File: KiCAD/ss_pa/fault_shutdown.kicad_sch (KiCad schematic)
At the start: 0 parts

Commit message: KiCad revC: ss_pa fault_shutdown populated + CD74HC4066 symbol + doc
Fault_shutdown sheet implemented with the self-latching V_REF scheme:
- LM393 (U1) powered from +3.3V (via RJ45 pin 6 from analog board)
- V_REF divider (R11=100K, R10=10K) powered from FAULT_N bus, giving
  intrinsic self-latching when fault asserts (no flip-flop needed) —
  normal V_REF ≈ 288 mV, fault V_REF = 0
- Pullup R9 (4.7K) on FAULT_N to +3.3V, wire-OR of both LM393 outputs
- FAULT_N is active-low (user renamed from FAULT after wire-OR polarity
  analysis — open-collector wire-OR of multiple fault sources requires
  LOW = fault for proper OR behavior)
- Startup cap C12 (1uF) + D1 (1N4148, cathode to V_REF) auto-resets
  the latch at power-on without needing button press
- CD74HC4066 (U2) in series with Bias_A/Bias_B lines — control pins
  tied to FAULT_N (HIGH=closed, LOW=open). Series-pass approach
  (not shunt-to-GND) avoids loading the MCP4728 DAC during a latched
  fault
- Reset: J5 screw terminal for external pushbutton; shorts +3.3V to
  V_REF momentarily to break the latch
- Noise filtering: C11 (0.01uF) on FAULT_N bus; C14/C15 (0.1uF each)
  bypass caps for U1 and U2
- RJ45 J7 (Amphenol RJE1D-188 shielded 8P8C) per T568B pair plan;
  shield grounded on PA-board end only

PA stage additions since last commit:
- L5 (12 uH on FT50-43, 5-6 turns) — supply input RFC between J2
  power entry and the +13.8V bus (L201-equivalent per QRP Labs kit)
- Fixed earlier wiring bugs flagged in review: U1 pin 6 moved from
  Source_Sense_A to Source_Sense_B so comparator B monitors Q4; C13
  replaced by C15 wired correctly as U2 bypass cap

Library:
- Added CD74HC4066 symbol (PDIP-14) to xmitter.kicad_sym with
  TI-style pinout; footprint = Package_DIP:DIP-14_W7.62mm

Documentation:
- Documentation/ss_pa.md rewritten to reflect as-built design:
  updated RJ45 pin assignment (pin 6 = +3.3V, pin 3 = FAULT_N),
  added L5 to supply decoupling, full rewrite of fault_shutdown
  section with the self-latchi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
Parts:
- added C11: 0.01uF, symbol Device:C
- added C12: 1uF, symbol Device:C
- added C14, C15: 0.1uF, symbol Device:C
- added D1: 1N4148, Diode_THT:D_DO-35_SOD27_P7.62mm_Horizontal, symbol Diode:1N4148
- added J5: Screw_Terminal_01x02, symbol Connector:Screw_Terminal_01x02
- added J7: 8P8C_Shielded, xmitter:Amphenol_RJE1D-188_Horizontal_Shielded, symbol Connector:8P8C_Shielded
- added R10: 10K, symbol Device:R_US
- added R11: 100K, symbol Device:R_US
- added R9: 4.7K, symbol Device:R_US
- added U1: LM393, symbol Comparator:LM393
- added U2: CD74HC4066, Package_DIP:DIP-14_W7.62mm, symbol xmitter:CD74HC4066
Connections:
- new net: C12.1, D1.2 (A)
- new net +3.3V: C12.2, C14.2, C15.2, J5.1 (Pin_1), J7.6, R9.1, U1.8 (V+), U2.14 (VCC)
- new net Bias_A: U2.2 (1Z)
- new net Bias_A_Raw: J7.7, U2.1 (1Y)
- new net Bias_B: U2.3 (2Z)
- new net Bias_B_Raw: J7.8, U2.4 (2Y)
- new net FAULT_N: C11.1, J7.3, R11.1, R9.2, U1.1, U1.7, U2.13 (1E), U2.5 (2E)
- new net GND: C11.2, C14.1, C15.1, J7.2, J7.5, J7.SH, R10.2, U1.4 (V-), U2.10 (4Z), U2.11 (4Y), U2.12 (4E), U2.6 (3E), U2.7 (GND), U2.8 (3Y), U2.9 (3Z)
- new net Source_Sense_A: J7.1, U1.2 (-)
- new net Source_Sense_B: J7.4, U1.6 (-)
- new net V_REF: D1.1 (K), J5.2 (Pin_2), R10.1, R11.2, U1.3 (+), U1.5 (+)
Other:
- note added: "If either source exceeds V_REF FAULT_N goes low"
- note added: "To pushbutton for manual reset"

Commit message: revC: accumulated schematic/netlist updates + BOM tooling
- analog + ss_pa netlists regenerated to current schematic state
- interface/arduino/dac/power sheet updates on analog
- fault_shutdown and pa_stage edits on ss_pa (footprint assignments)
- assign_cap_footprints.py: additional VALUE_TO_FOOTPRINT entries
- gen_board_boms.py: per-board BOM generator (multi-sheet .xlsx by
  component category, first-match-wins bucketing, DNP exclusion)
- gen_total_bom.py: consolidated BOM across analog + frontpanel + ss_pa
  for a single Mouser order, board-prefixed references, mixed-footprint
  flagging per Value row

Co-Authored-By: Claude Opus 4.7 <noreply@anthropic.com>
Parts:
- C11: footprint (none) -> Capacitor_THT:C_Disc_D6.0mm_W2.5mm_P5.00mm
- C12: footprint (none) -> Capacitor_THT:C_Rect_L7.2mm_W4.5mm_P5.00mm
- C14, C15: footprint (none) -> Capacitor_THT:C_Disc_D5.0mm_W2.5mm_P5.00mm
- J5: footprint (none) -> TerminalBlock_Phoenix:TerminalBlock_Phoenix_MKDS-1,5-2_1x02_P5.00mm_Horizontal
- R10, R11, R9: footprint (none) -> Resistor_THT:R_Axial_DIN0207_L6.3mm_D2.5mm_P10.16mm_Horizontal
- U1: footprint (none) -> Package_DIP:DIP-8_W7.62mm
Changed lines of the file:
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@@
 			)
 		)
-		(property "Footprint" ""
+		(property "Footprint" "Package_DIP:DIP-8_W7.62mm"
 			(at 115.57 129.54 0)
 			(hide yes)
@@
 			)
 		)
-		(property "Footprint" ""
+		(property "Footprint" "Capacitor_THT:C_Disc_D6.0mm_W2.5mm_P5.00mm"
 			(at 136.8552 156.21 0)
 			(hide yes)
@@
 			)
 		)
-		(property "Footprint" ""
+		(property "Footprint" "Capacitor_THT:C_Disc_D5.0mm_W2.5mm_P5.00mm"
 			(at 107.95 142.5448 0)
 			(hide yes)
@@
 			)
 		)
-		(property "Footprint" ""
+		(property "Footprint" "Resistor_THT:R_Axial_DIN0207_L6.3mm_D2.5mm_P10.16mm_Horizontal"
 			(at 131.826 109.474 90)
 			(hide yes)
@@
 			)
 		)
-		(property "Footprint" ""
+		(property "Footprint" "Capacitor_THT:C_Rect_L7.2mm_W4.5mm_P5.00mm"
 			(at 172.4152 158.75 0)
 			(hide yes)
@@
 			)
 		)
-		(property "Footprint" ""
+		(property "Footprint" "Package_DIP:DIP-8_W7.62mm"
 			(at 114.3 151.13 0)
 			(hide yes)
@@
 			)
 		)
-		(property "Footprint" ""
+		(property "Footprint" "TerminalBlock_Phoenix:TerminalBlock_Phoenix_MKDS-1,5-2_1x02_P5.00mm_Horizontal"
 			(at 185.42 140.97 0)
 			(hide yes)
@@
 			)
 		)
-		(property "Footprint" ""
+		(property "Footprint" "Resistor_THT:R_Axial_DIN0207_L6.3mm_D2.5mm_P10.16mm_Horizontal"
 			(at 143.764 147.574 90)
 			(hide yes)
@@
 			)
 		)
-		(property "Footprint" ""
+		(property "Footprint" "Capacitor_THT:C_Disc_D5.0mm_W2.5mm_P5.00mm"
 			(at 160.9852 69.85 0)
 			(hide yes)
@@
 			)
 		)
-		(property "Footprint" ""
+		(property "Footprint" "Package_DIP:DIP-8_W7.62mm"
 			(at 115.57 113.03 0)
 			(hide yes)
@@
 			)
 		)
-		(property "Footprint" ""
+		(property "Footprint" "Resistor_THT:R_Axial_DIN0207_L6.3mm_D2.5mm_P10.16mm_Horizontal"
 			(at 150.876 153.924 90)
 			(hide yes)

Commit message: revD: DGFET-DAC bias scheme, kit-style xfmr naming, custom footprints, Output LPF project
Architecture refinements since the previous revD commit (f8d7058):

Analog board (vfo_complete, arduino, dac, power sheets):
  * MCP4922 (U4) ch B exposed as DRIVER_BIAS DAC output -> J31 pin 6
    (replaces the +3.3V pin that was on J31 pin 6 before). Analog's U4
    now controls the ss_pa BS170 driver DC bias point directly from
    firmware -- cleaner than the kit's trimmer+Q201 scheme.
  * MCP4728 (U3) ch A/B exposed as PA_Bias_A_Raw / PA_Bias_B_Raw ->
    J31 pins 7, 8. These feed the ss_pa CD74HC4066 fault-switch (U2),
    which gates them to PA_Bias_A/B on the IRF510 gates. On FAULT_N
    low, switch opens -> IRF510 bias collapses -> conduction cuts.
  * Rename pass: Bias_A/B/_Raw labels -> PA_Bias_A/B/_Raw everywhere
    (analog J3 screw-terminal, umbilical J31, ss_pa U2 inputs). Prefix
    disambiguates from DRIVER_BIAS which drives a different stage.
  * J2 (band-select RJ45 to Output LPF board): added RLY_40 provision.
    Pin layout reorganized -- RLY_40 lives at pin 5, pin 6 kept as a
    spare for a future 6th band.

ss_pa board (pa_stage, fault_shutdown, lpf sheets):
  * Driver + final BS170/IRF510 topology drawn following QRP Labs
    10W Linear kit (RF IN -> T201 input xfmr -> BS170 PP driver
    (Q2, Q6) -> T202 interstage -> IRF510 PP finals (Q3, Q4) ->
    T203 bifilar drain feed -> T204 output xfmr -> RF out).
  * Transformer references renamed to match the kit: T201 (input,
    BN61-2402), T202 (interstage, BN61-2402), T203 (drain feed,
    T50-43), T204 (output, BN43-202).
  * Driver bias filter on DRIVER_BIAS: C19 (0.1uF) + C20 (100pF)
    bulk + HF bypass, into T201 secondary CT (pin 4).
  * +3.3V now locally regulated on ss_pa (MCP1700x-330xxTO, U13)
    from +13.8V, powering U1 (LM393) and U2 (CD74HC4066). J31
    pin 6 freed up for DRIVER_BIAS.
  * Duplicate RJ45 J7 deleted (was a leftover from pre-DAC-bias era).
  * J3 (SMA RF input from analog) foo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
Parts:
- removed J7: 8P8C_Shielded, xmitter:Amphenol_RJE1D-188_Horizontal_Shielded, symbol Connector:8P8C_Shielded
- added C16, C21: 1uF, Capacitor_THT:C_Rect_L7.2mm_W4.5mm_P5.00mm, symbol Device:C_US
- added R12, R19: 100K, Resistor_THT:R_Axial_DIN0207_L6.3mm_D2.5mm_P10.16mm_Horizontal, symbol Device:R_US
- added U13: MCP1700x-330xxTO, Package_TO_SOT_THT:TO-92_Inline_Wide, symbol Regulator_Linear:MCP1700x-330xxTO
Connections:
- net +3.3V: now also C21.1, U13.3 (VO)
- net GND: now also C16.2, C21.2, R12.2, R19.1, U13.1 (GND)
- net Bias_A renamed PA_Bias_A
- net PA_Bias_A: now also R19.2
- net Bias_A_Raw renamed PA_Bias_A_Raw
- net Bias_B renamed PA_Bias_B
- net PA_Bias_B: now also R12.1
- net Bias_B_Raw renamed PA_Bias_B_Raw
- new net +13.8V: C16.1, U13.2 (VI)

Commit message: revD ss_pa: add test points (drains + RF out + bias + supply), 4-layer PCB
ss_pa test points added:
  TP1  +3.3V          - local U13 LDO output monitor
  TP2  PA_Bias_A      - IRF510 Q3 bias after fault switch (R12 pulldown)
  TP3  PA_Bias_B      - IRF510 Q4 bias after fault switch (R19 pulldown)
  TP4  (unconnected)  - orphan pad, clean up in next pass
  TP5  RF OUT         - J1 center pin, final 50 ohm matched RF out
  TP6  Q3 drain       - hot RF, oscillation check pad
  TP7  Q4 drain       - hot RF, oscillation check pad
  TP8  GND            - probe-return pad near one hot-RF TP
  TP9  GND            - probe-return pad near other hot-RF TP

Deliberately minimal set per earlier RF-stability discussion:
  * No TPs on BS170 drains, IRF510 gates, driver sources, or J3 RF
    input -- would require longer stubs that risk disturbing the
    VHF-tuned drain-gate feedback network. Mini-grabber on the
    device lead during bring-up is cleaner than a permanent pad.
  * Hot-RF TPs (TP5/6/7) are small-pad / short-stub.
  * Each hot-RF TP is paired with a nearby GND pad (TP8, TP9) so
    scope-probe ground spring reaches directly -- short probe loop
    for clean HF waveform, no antenna pickup.

4-layer PCB stackup planned for ss_pa (not 2-layer):
  * Outer layers: signal + GND pour
  * Inner layer 2: solid GND plane (uninterrupted)
  * Inner layer 3: solid +13.8 V plane (uninterrupted)
  * Via-stitching ties outer GND pours to inner GND plane
Benefits: cleaner RF return currents under driver + final chain,
lower-impedance power distribution for IRF510 pulse currents
(~2 A peak each), better heat spreading through +13.8 V plane
under the drain-feed region, reduced EMI radiation.

Docs updated:
  * Documentation/test_points.md -- added full ss_pa TP section
    with bring-up workflow (power-on sanity check, oscillation
    check, fault chain verification, RF level check). Doc title
    changed to cover both boards.
  * Documentation/Master_Description.md -- ss_pa section n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
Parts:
- added TP1, TP2, TP3: xTP, Connector_PinHeader_2.54mm:PinHeader_1x01_P2.54mm_Vertical, symbol xmitter:xTP
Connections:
- net +3.3V: now also TP1.1
- net PA_Bias_A: now also TP2.1
- net PA_Bias_B: now also TP3.1
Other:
- moved on the sheet: R12, R19

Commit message: revD: address PDF design-review items M2-M4 + archive review handoff
- Fix schematic issues M2-M4 flagged in the pre-layout design review:
  changes in KiCAD/analog/vfo_complete.kicad_sch and
  KiCAD/ss_pa/fault_shutdown.kicad_sch. M1 is a documentation-only
  item and does not require a schematic edit.
- Regenerate netlists for analog, ss_pa, Output LPF, frontpanel,
  protoshield.
- Add Documentation/revD_prelayout_review_handoff.md -- the handoff
  package used to brief the external reviewer (board-by-board summary,
  cross-board interconnects, specific review asks).
- Add Documentation/xmitter Rev D Pre-Layout Design Review-1.pdf --
  the reviewer's returned analysis, kept for traceability of future
  changes against the Must-Fix / Should-Consider / Nice-to-Have items.

Co-Authored-By: Claude Opus 4.7 <noreply@anthropic.com>
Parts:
- U13: value MCP1700x-330xxTO -> LM2936Z-3.3/NOPB
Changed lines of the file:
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@@
 			)
 		)
-		(property "Value" "MCP1700x-330xxTO"
+		(property "Value" "LM2936Z-3.3/NOPB"
 			(at 217.17 82.55 0)
 			(show_name no)

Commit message: revD: ss_pa Option C 5V rail + analog SW1 THT + R/C footprints + doc refresh
ss_pa Option C: swap U13 to LM2936Z-5.0 (full +5V logic rail), re-size
R10 10K->6.8K to preserve ~0.3V fault trip at new rail, drop +3.3V net
entirely. Fixes the previously-dead +5V bus that had no source.

Analog SW1 (Si5351 bringup DPDT): swap SMD footprint for
Button_Switch_THT:SW_CK_JS202011CQN_DPDT_Straight. Verified pin-numbering
convention (pin 1 above pin 6 in THT) matches user's intended DPST
wiring; both SDA/SCL break together.

Analog: assign missing footprints to R3/R4/R5/R8/R9 (DIN0207 axial) and
C4/C5/C6/C7/C8 (disc ceramic 5mm). Add xmitter:DIP-14_W7.62mm.kicad_mod
and 74HCT125 symbol to the xmitter library.

Documentation: Rev D handoff doc updated with M1-M8 fix status, Option C
notes, I2C bus voltage architecture, 74HCT125 SPI shifter, FAULT_N
divider details, and Metro-no-footprint note. Supporting docs updated:
i2c_bus.md full rewrite for 5V HV bus + STEMMA reroute, revD_interconnect
board inventory refresh, status banners on ss_pa.md / Master_Description /
cw_envelope_keyer / front_panel_interface pointing to handoff doc for
items beyond their last-current date.

Co-Authored-By: Claude Opus 4.7 <noreply@anthropic.com>
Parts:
- added C19: 0.1uF, Capacitor_THT:C_Disc_D5.0mm_W2.5mm_P5.00mm, symbol Device:C
- added C20: 100pF, Capacitor_THT:C_Rect_L7.0mm_W3.5mm_P5.00mm, symbol Device:C
- added J31: 8P8C_Shielded, xmitter:Amphenol_RJE1D-188_Horizontal_Shielded, symbol Connector:8P8C_Shielded
- R10: value 10K -> 6.8K
- U13: value LM2936Z-3.3/NOPB -> LM2936Z-5.0/NOPB
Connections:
- net FAULT_N: now also J31.3
- net GND: now also C19.2, C20.2, J31.2, J31.5, J31.SH
- net PA_Bias_A_Raw: now also J31.7
- net PA_Bias_B_Raw: now also J31.8
- net Source_Sense_A: now also J31.1
- net Source_Sense_B: now also J31.4
- net +3.3V renamed +5V
- new net DRIVER_BIAS: C19.1, C20.1, J31.6

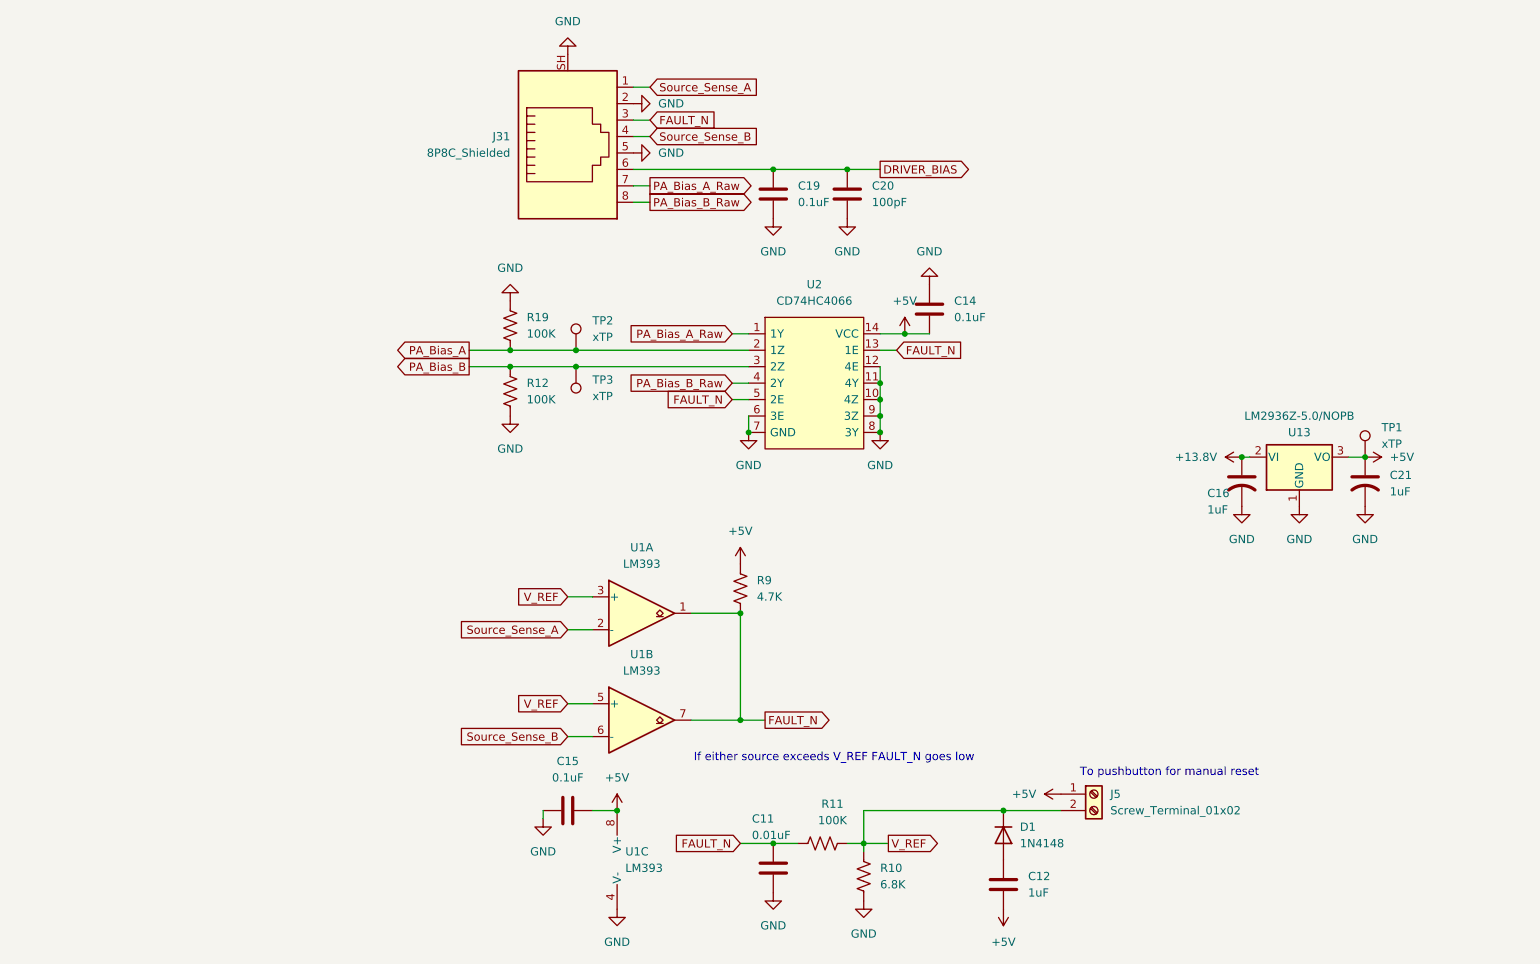
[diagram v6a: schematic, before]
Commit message: revD: analog + ss_pa RF filtering on umbilical signals
ss_pa: 1 uH RFC + bypass cap(s) added on each umbilical-crossing signal
to attenuate 14 MHz ingress from the cable and keep hot IRF510-source
RF from being injected back into the umbilical:

- PA_Bias_A_Raw: L6 1uH + C13 100nF + C26 100pF at J31.7
- PA_Bias_B_Raw: L7 1uH + C22 100nF + C27 100pF at J31.8
- Source_Sense_A: L8 1uH + C23 100nF between IRF510A source tap and
  the shared comparator/ADC node (new Source_Sense_A_Raw holds the
  Kelvin sense resistors R1/R2)
- Source_Sense_B: L9 1uH + C24 100nF, mirror of A on Q4 side
- DRIVER_BIAS: R20 100R + C19 0.1uF + C20 100pF already placed
  previously
- FAULT_N: R23 100R + C25 100pF filter on the external side of the
  latch (LM393 outputs + R9 pullup remain on the internal node for
  fast latching, R23 isolates from umbilical and 4066 enables)

Attenuation ~40-60 dB at 14 MHz across all five umbilical signals.

Analog: companion schematic touches for the DGFET G2 op-amp mute
subcircuit on the test sheet.

Co-Authored-By: Claude Opus 4.7 <noreply@anthropic.com>
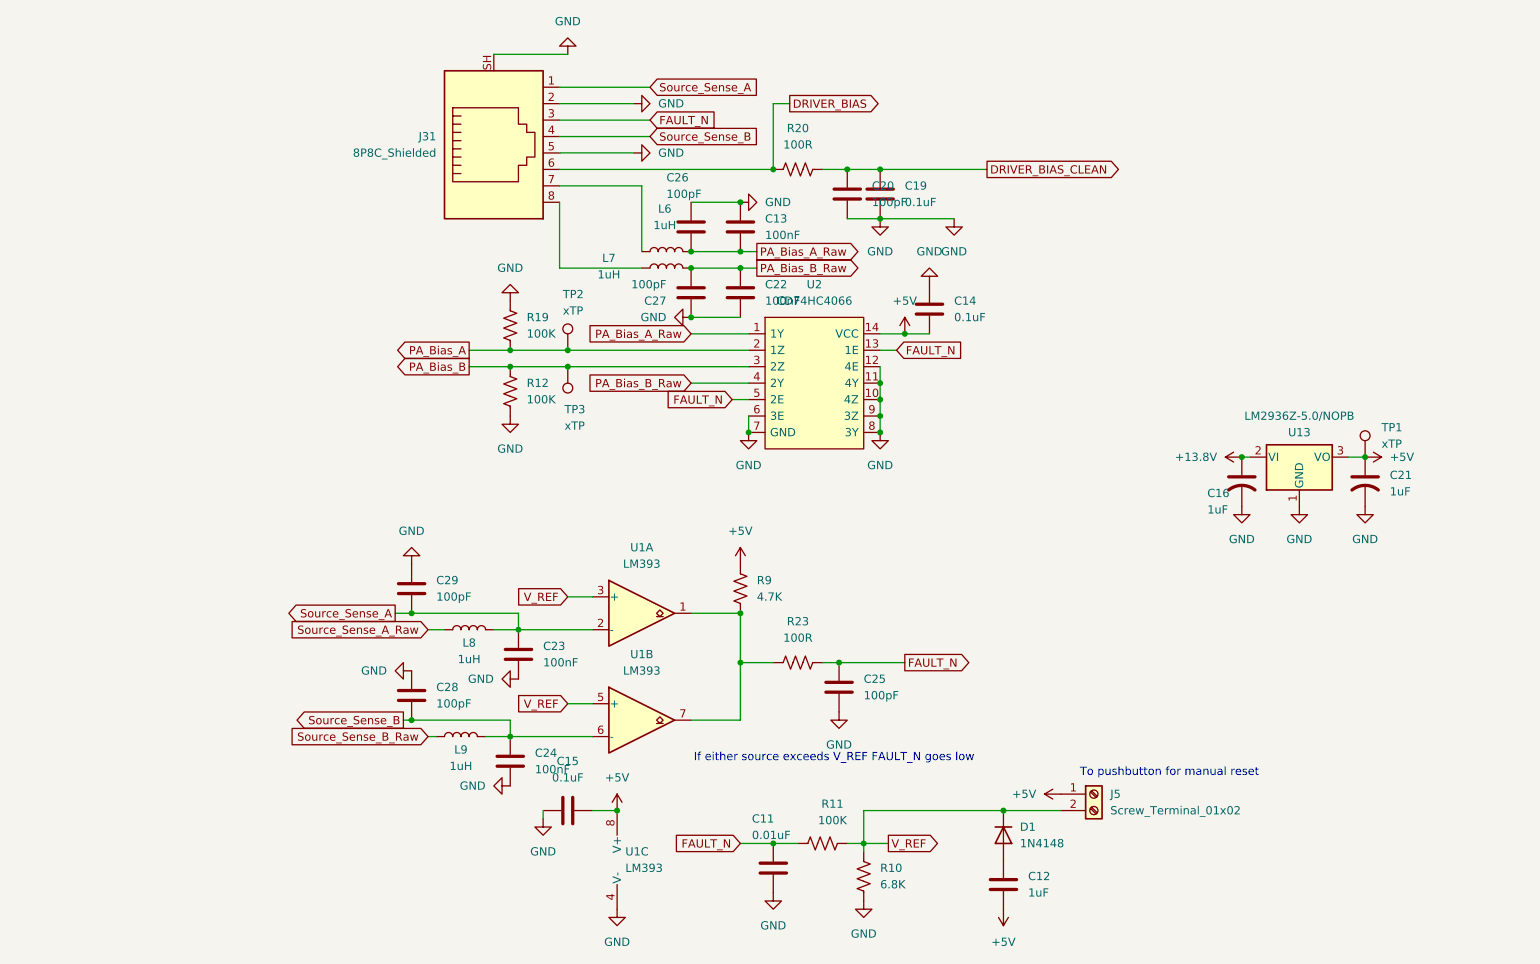
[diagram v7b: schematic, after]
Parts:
- added C13, C22, C23, C24: 100nF, symbol Device:C
- added C25, C26, C27, C28, C29: 100pF, symbol Device:C
- added L6, L7, L8, L9: 1uH, Inductor_THT:L_Axial_L5.3mm_D2.2mm_P2.54mm_Vertical_Vishay_IM-1, symbol Device:L
- added R20, R23: 100R, symbol Device:R_US
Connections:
- net DRIVER_BIAS: now also R20.1; no longer C19.1, C20.1
- net FAULT_N: now also C25.1, R23.2; no longer R9.2, U1.1, U1.7
- net GND: now also C13.1, C22.2, C23.2, C24.2, C25.2, C26.1, C27.1, C28.1, C29.1
- net PA_Bias_A_Raw: now also C13.2, C26.2, L6.2; no longer J31.7
- net PA_Bias_B_Raw: now also C22.1, C27.2, L7.2; no longer J31.8
- net Source_Sense_A: now also C23.1, C29.2, L8.2
- net Source_Sense_B: now also C24.1, C28.2, L9.2
- new net: R23.1, R9.2, U1.1, U1.7
- new net: J31.7, L6.1
- new net: J31.8, L7.1
- new net DRIVER_BIAS_CLEAN: C19.1, C20.1, R20.2
- new net Source_Sense_A_Raw: L8.1
- new net Source_Sense_B_Raw: L9.1
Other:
- moved on the sheet: C19, J31, TP2, TP3
